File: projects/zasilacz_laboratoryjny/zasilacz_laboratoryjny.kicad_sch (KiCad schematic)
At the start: 33 parts, among them J1 Conn_Point, J2 Conn_Point, J3 Conn_Point, J4 Conn_Point, P1 10kΩ, T1 BC557, T2 BC557, T3 BC547, T4 BC547, T5 BC557, U1 DB207, U2 LM317, U3 Voltmeter_digital, Y1 Buzzer_Piezo_Active

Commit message: zasilacz laboratoryjny v2.0
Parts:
- removed R3: 10kΩ, symbol *Custom_Generic:R
- removed Y1: Buzzer_Piezo_Active, symbol *Custom_Generic:Buzzer_Piezo_Active
- added D4: Yellow, symbol *Custom_Generic:LED
- added T6: BC557, symbol *Custom_Generic:PNP_BJT_BCE
- added Y1: 3V, symbol *Custom_Generic:Buzzer_Magnetic_Active
- D1: value 5V6 -> 3V6
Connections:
- net GNDD: now reaches C1.1 (-), C2.1 (-), C3.2, D3.1 (K), R1.2, R11.2, R5.2, T2.2 (C), T4.3 (E), U1.2 (−)
- net GNDD: now also T6.2 (C); no longer U3.2 (GND)
- net VDC: now reaches C1.2 (+), R4.1, T1.3 (E), U1.1 (+), U2.3 (VI)
- net VDC: now also D1.1 (K), U3.2 (PWR), Y1.1; no longer R2.1, U3.1 (PWR)
- net at C2.2 (+), D2.2 (A): now also R2.2, D4.2 (A); no longer D1.2 (A), T3.1 (C)
- net at C5.2 (+), J3.1 (Pin_1), R10.1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: now also U3.1 (SENSE); no longer U3.3 (SENSE)
- net at C4.1 (-), C5.1 (-), J4.1 (Pin_1)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: now also U3.3 (GND)
- new net: T6.3 (E), Y1.2
- new net: D1.2 (A), R2.1, T6.1 (B)
- new net: D4.1 (K), T3.1 (C)
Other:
- moved on the sheet: C1, C2, C3, C4, C5, D1, D2, D3, P1, R1, R10, R11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

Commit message: Wersja 2.0 po modyfikacjach wynikłych z testowania
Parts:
- added D5: 1N4007, symbol *Custom_Generic:D
- added R12, R3: 10kΩ, symbol *Custom_Generic:R
- added R13, R14: 1kΩ, symbol *Custom_Generic:R
- added T7: BC517, symbol *Custom_Generic:NPN_Darlington_CBE
- added T8: BC547, symbol *Custom_Generic:NPN_BJT_CBE
- C2: value 22μF/25V -> 100μF/25V
- D1: value 3V6 -> 1N4729
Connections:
- net at D2.2 (A), R2.2: no longer C2.2 (+), D4.2 (A)
- net at D1.2 (A), R2.1, T6.1 (B): now also R13.1
- net at R5.1, T3.3 (E), T4.2 (B): now also T8.2 (B)
- net at D4.1 (K): now also T8.1 (C); no longer T3.1 (C)
- net GNDD renamed GND
- net GND: now also R12.2, T8.3 (E)
- net VDC renamed V1
- net V1: now also D5.1 (K), R14.1, T7.1 (C); no longer D1.1 (K), U1.1 (+), U3.2 (PWR), Y1.1
- new net: D4.2 (A), R13.2
- new net: D5.2 (A), R3.1, U1.1 (+)
- new net: R12.1, R3.2, T7.2 (B)
- new net: R14.2, T3.1 (C)
- new net V3: C2.2 (+), D1.1 (K), T7.3 (E), U3.2 (PWR), Y1.1
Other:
- moved on the sheet: C1, C3, C4, C5, D1, D2, D3, D4, P1, R1, R10, R11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

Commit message: preparations for board design in VeeCAD
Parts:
- removed R11: Current sense, symbol *Custom_Generic:R
- added R14, R15: 75Ω, VeeCad:AX3_1N, symbol *Custom_Generic:R
- added R16, R17: 10Ω, VeeCad:AX3_1N, symbol *Custom_Generic:R
- added R18, R19: 22Ω, VeeCad:AX3_1N, symbol *Custom_Generic:R
- added R20: 5,6Ω, VeeCad:AX3_1N, symbol *Custom_Generic:R
- added R21: 2,2Ω, VeeCad:AX3_1N, symbol *Custom_Generic:R
- added R22: 3,9Ω, VeeCad:AX6_2N, symbol *Custom_Generic:R
- added R23: 1Ω, VeeCad:AX6_2N, symbol *Custom_Generic:R
- added R24: 2Ω, VeeCad:AX6_2N, symbol *Custom_Generic:R
- added R25: 0,33Ω, VeeCad:AX6_2N, symbol *Custom_Generic:R
- added R26: 1,5Ω, VeeCad:AX6_2N, symbol *Custom_Generic:R
- added R27: 0Ω, VeeCad:AX1_1N, symbol *Custom_Generic:R
- added SW1: SW_SP8T, VeeCad:SIP9, symbol *Custom_Generic:SW_SP8T
- added SW2: SW_SPST, VeeCad:SIP2, symbol *Custom_Generic:SW_SPST
- C1: footprint (none) -> VeeCad:RA3_6
- C2, C4: footprint (none) -> VeeCad:RA1_2
- C3: footprint (none) -> VeeCad:AX2_1N
- C5: footprint (none) -> VeeCad:RA1_3
- D1, D5: footprint (none) -> VeeCad:AX2_1
- D2, D3, D4: footprint (none) -> VeeCad:SIP2
- J1, J2, J3, J4: footprint (none) -> VeeCad:SIP1
- P1, U3: footprint (none) -> VeeCad:SIP3
- R1, R10, R13, R2, R3, R4, R5, R6, R7, R8, R9: footprint (none) -> VeeCad:AX3_1N
- R11: renamed from R14; footprint (none) -> VeeCad:AX3_1N
- R12: value 10kΩ -> 220kΩ; footprint (none) -> VeeCad:AX3_1N
- T1, T2, T3, T4, T5, T6, T7, T8: footprint (none) -> VeeCad:TO92
- U1: footprint (none) -> VeeCad:DIP4_6
- U2: footprint Package_TO_SOT_THT:TO-220-3_Vertical -> VeeCad:TO220
- Y1: footprint (none) -> VeeCad:BUZR_12
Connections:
- net GND: now also U1.4 (−), R14.2, R15.2, R17.2, R18.2, R19.2, R21.2, R23.2, R25.2, R26.2, R27.2; no longer U1.2 (−)
- net at C4.1 (-), C5.1 (-), J4.1 (Pin_1)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: now also SW1.1
- net at D5.2 (A), R3.1: now also U1.3 (+); no longer U1.1 (+)
- net at J2.1 (Pin_1): now also SW2.2 (B1); no longer U1.4 (∼)
- net at J1.1 (Pin_1): now also U1.1 (∼); no longer U1.3 (∼)
- new net: R20.1, SW1.5
- new net: R20.2, R21.1
- new net: R27.1, SW1.9
- new net: R18.1, R19.1, SW1.4
- new net: R14.1, R15.1, SW1.2
- new net: SW2.1 (A1), U1.2 (∼)
- new net: R24.1, SW1.7
- new net: R24.2, R25.1
- new net: R22.1, SW1.6
- new net: R22.2, R23.1
- new net: R26.1, SW1.8
- new net: R16.2, R17.1
- new net: R16.1, SW1.3
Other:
- note added: "100mA"
- note added: "150mA"
- note added: "20mA"
- note added: "250mA"
- note added: "500mA"
- note added: "50mA"
- note added: "750mA"
- note added: "AC / DC"
- note added: "No OCP"
- note removed: "AC 12V"
- moved on the sheet: C1, C2, C3, C4, C5, D1, D2, D3, D4, D5, P1, R1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

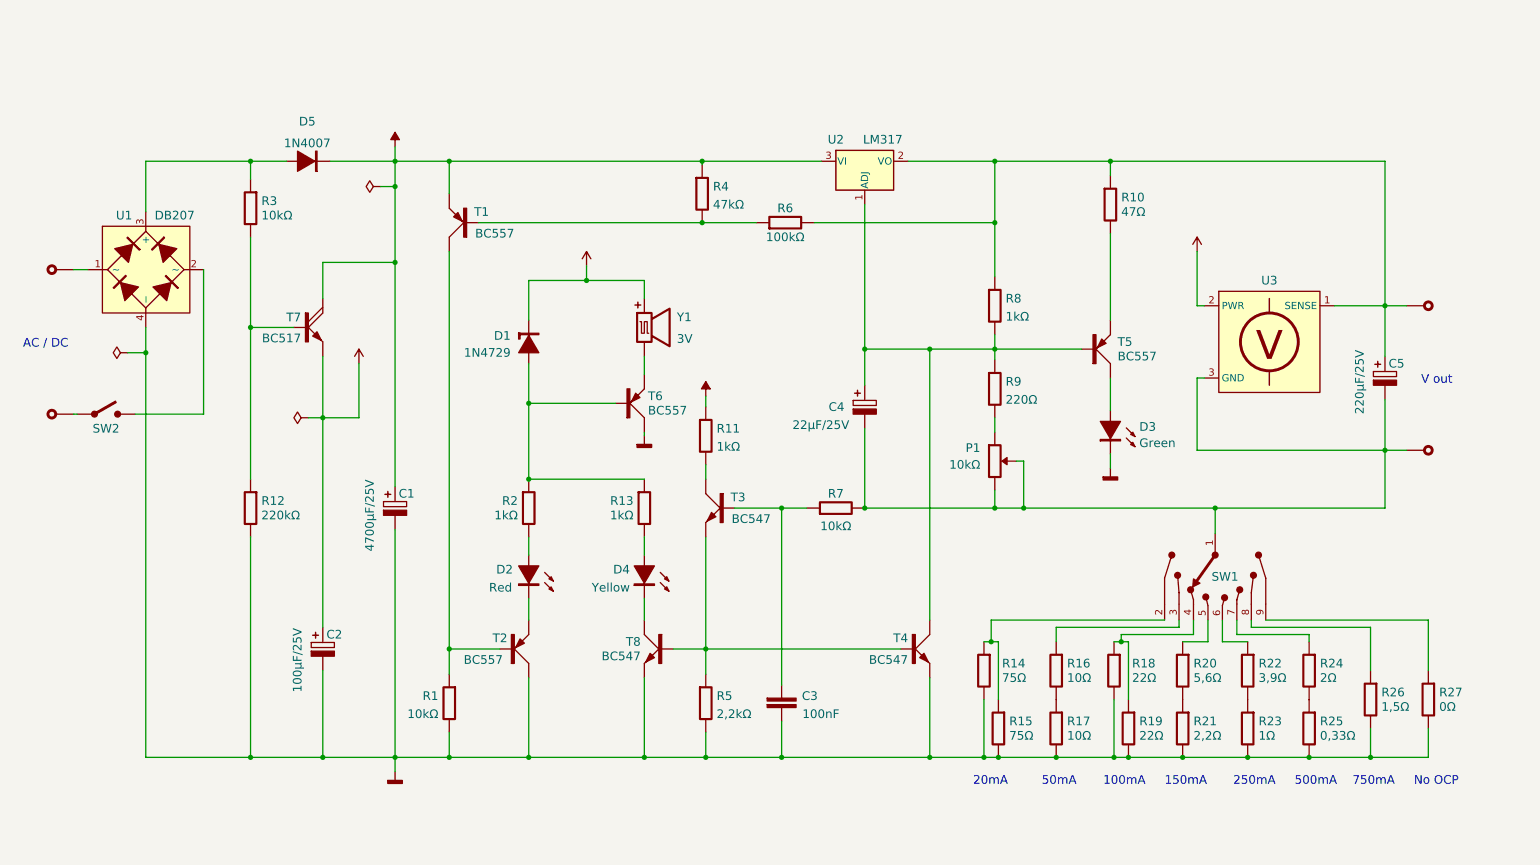
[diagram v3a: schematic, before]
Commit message: started veecad layout for zasilacz_laboratoryjny, some small stuff elsewhere
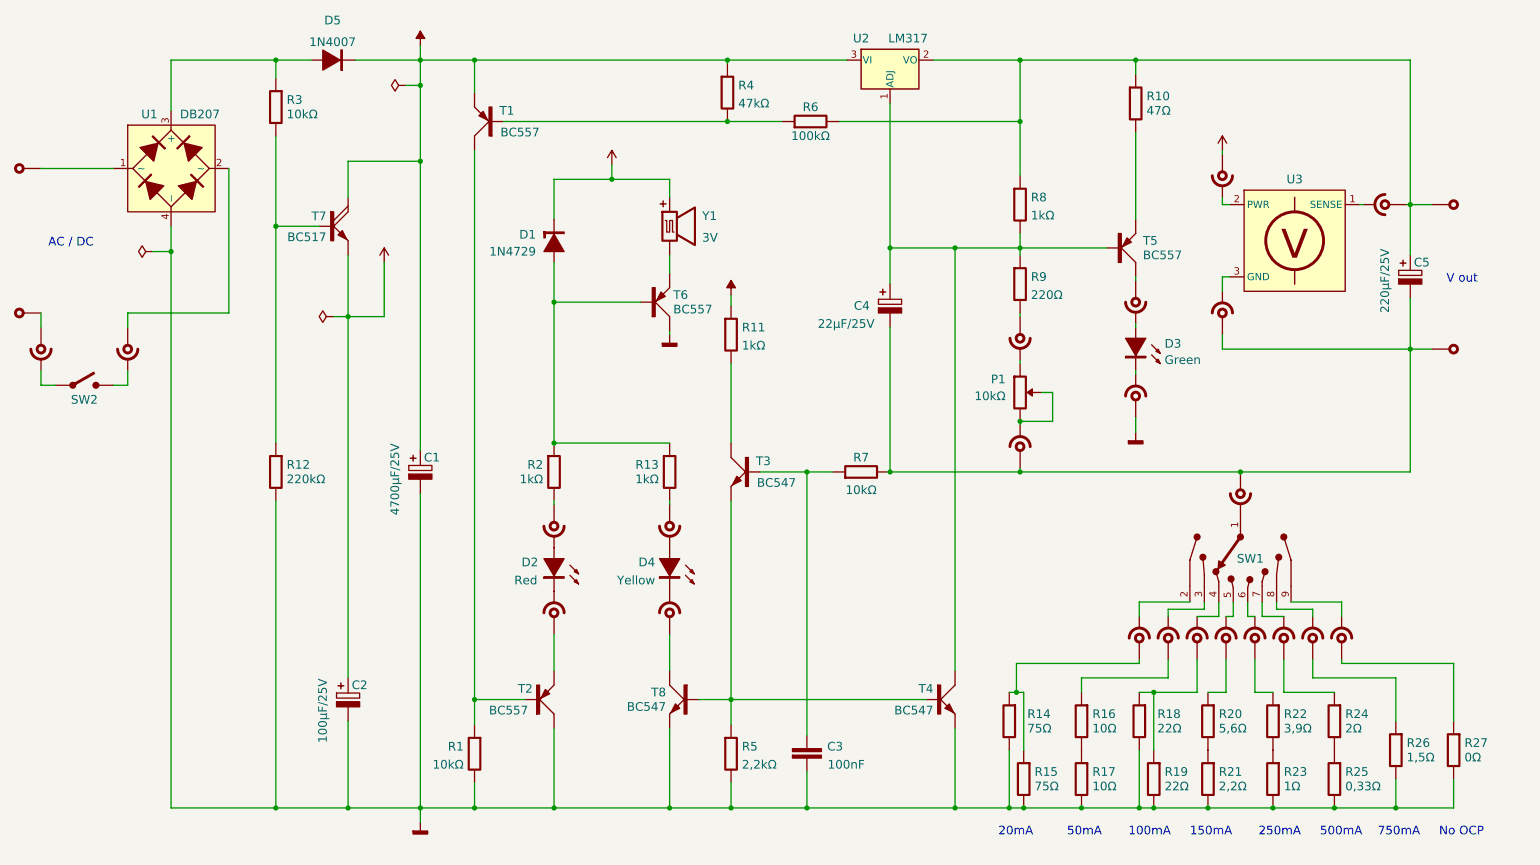
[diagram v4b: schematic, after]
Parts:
- added J10: VDO_LED+, VeeCad:SIP1, symbol *Custom_Generic:Conn_Point_M
- added J11, J14, J15, J17, J19, J21, J24, J26, J28, J29, J31, J33, J35, J37, J39, J41, J43, J46, J48, J5, J8, J9: Conn_Point_1, symbol *Custom_Generic:Conn_Point_F
- added J12: VDO_LED−, VeeCad:SIP1, symbol *Custom_Generic:Conn_Point_M
- added J13: OCP_LED+, VeeCad:SIP1, symbol *Custom_Generic:Conn_Point_M
- added J16: OCP_LED−, VeeCad:SIP1, symbol *Custom_Generic:Conn_Point_M
- added J18: VPOT_1, VeeCad:SIP1, symbol *Custom_Generic:Conn_Point_M
- added J20: VPOT_2, VeeCad:SIP1, symbol *Custom_Generic:Conn_Point_M
- added J22: PWR_LED+, VeeCad:SIP1, symbol *Custom_Generic:Conn_Point_M
- added J23: PWR_LED−, VeeCad:SIP1, symbol *Custom_Generic:Conn_Point_M
- added J25: OCP_SW1, VeeCad:SIP1, symbol *Custom_Generic:Conn_Point_M
- added J27: OCP_SW2, VeeCad:SIP1, symbol *Custom_Generic:Conn_Point_M
- added J30: OCP_SW3, VeeCad:SIP1, symbol *Custom_Generic:Conn_Point_M
- added J32: VM_PWR, VeeCad:SIP1, symbol *Custom_Generic:Conn_Point_M
- added J34: VM_GND, VeeCad:SIP1, symbol *Custom_Generic:Conn_Point_M
- added J36: OCP_SW4, VeeCad:SIP1, symbol *Custom_Generic:Conn_Point_M
- added J38: OCP_SW_IN, VeeCad:SIP1, symbol *Custom_Generic:Conn_Point_M
- added J40: OCP_SW5, VeeCad:SIP1, symbol *Custom_Generic:Conn_Point_M
- added J42: OCP_SW6, VeeCad:SIP1, symbol *Custom_Generic:Conn_Point_M
- added J44: OCP_SW7, VeeCad:SIP1, symbol *Custom_Generic:Conn_Point_M
- added J45: OCP_SW8, VeeCad:SIP1, symbol *Custom_Generic:Conn_Point_M
- added J47: VM_SEN, VeeCad:SIP1, symbol *Custom_Generic:Conn_Point_M
- added J6: PWR_SW1, VeeCad:SIP1, symbol *Custom_Generic:Conn_Point_M
- added J7: PWR_SW2, VeeCad:SIP1, symbol *Custom_Generic:Conn_Point_M
- C3: footprint VeeCad:AX2_1N -> VeeCad:AX1_1N
- D2, D3, D4, SW2: footprint VeeCad:SIP2 -> (none)
- J1, J2: value Conn_Point -> AC_IN; symbol *Custom_Generic:Conn_Point -> *Custom_Generic:Conn_Point_M
- J3: value Conn_Point -> VOUT+; symbol *Custom_Generic:Conn_Point -> *Custom_Generic:Conn_Point_M
- J4: value Conn_Point -> VOUT−; symbol *Custom_Generic:Conn_Point -> *Custom_Generic:Conn_Point_M
- P1, U3: footprint VeeCad:SIP3 -> (none)
- R16, R17, R20, R21: footprint VeeCad:AX3_1N -> VeeCad:VERTAX_1N
- R22, R23, R24, R25, R26: footprint VeeCad:AX6_2N -> VeeCad:VERTAX2_1N
- SW1: footprint VeeCad:SIP9 -> (none)
- U1: footprint VeeCad:DIP4_6 -> VeeCad:DIP4_DB
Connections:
- net GND: now also J23.1 (Pin_1); no longer D3.1 (K)
- net V3: now also J32.1 (Pin_1); no longer U3.2 (PWR)
- net at C5.2 (+), J3.1 (Pin_1), R10.1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: now also J47.1 (Pin_1); no longer U3.1 (SENSE)
- net at R20.1: now also J36.1 (Pin_1); no longer SW1.5
- net at R27.1: now also J45.1 (Pin_1); no longer SW1.9
- net at R18.1, R19.1: now also J30.1 (Pin_1); no longer SW1.4
- net at C4.1 (-), C5.1 (-), J4.1 (Pin_1)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: now also J20.1 (Pin_1), J34.1 (Pin_1), J38.1 (Pin_1); no longer P1.2, P1.3, SW1.1, U3.3 (GND)
- net at R14.1, R15.1: now also J25.1 (Pin_1); no longer SW1.2
- net at U1.2 (∼): now also J7.1 (Pin_1); no longer SW2.1 (A1)
- net at SW2.2 (B1): now also J5.1 (Pin_1); no longer J2.1 (Pin_1)
- net at R24.1: now also J42.1 (Pin_1); no longer SW1.7
- net at SW1.6: now also J39.1 (Pin_1); no longer R22.1
- net at T8.1 (C): now also J16.1 (Pin_1); no longer D4.1 (K)
- net at P1.1: now also J17.1 (Pin_1); no longer R9.2
- net at R13.2: now also J13.1 (Pin_1); no longer D4.2 (A)
- net at D3.2 (A): now also J21.1 (Pin_1); no longer T5.2 (C)
- net at D2.2 (A): now also J9.1 (Pin_1); no longer R2.2
- net at D2.1 (K): now also J11.1 (Pin_1); no longer T2.3 (E)
- net at SW1.8: now also J43.1 (Pin_1); no longer R26.1
- net at R16.1: now also J27.1 (Pin_1); no longer SW1.3
- new net: J31.1 (Pin_1), U3.2 (PWR)
- new net: J37.1 (Pin_1), SW1.1
- new net: J29.1 (Pin_1), SW1.4
- new net: J8.1 (Pin_1), SW2.1 (A1)
- new net: J40.1 (Pin_1), R22.1
- new net: J41.1 (Pin_1), SW1.7
- new net: J19.1 (Pin_1), P1.2, P1.3
- new net: J33.1 (Pin_1), U3.3 (GND)
- new net: J12.1 (Pin_1), T2.3 (E)
- new net: D3.1 (K), J24.1 (Pin_1)
- new net: D4.1 (K), J15.1 (Pin_1)
- new net: J10.1 (Pin_1), R2.2
- new net: J48.1 (Pin_1), U3.1 (SENSE)
- new net: J2.1 (Pin_1), J6.1 (Pin_1)
- new net: J35.1 (Pin_1), SW1.5
- new net: D4.2 (A), J14.1 (Pin_1)
- new net: J44.1 (Pin_1), R26.1
- new net: J18.1 (Pin_1), R9.2
- new net: J22.1 (Pin_1), T5.2 (C)
- new net: J28.1 (Pin_1), SW1.3
- new net: J26.1 (Pin_1), SW1.2
- new net: J46.1 (Pin_1), SW1.9
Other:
- moved on the sheet: C1, C2, C3, C4, C5, D1, D2, D3, D4, D5, P1, R1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

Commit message: beautify some symbols, power supply WIP
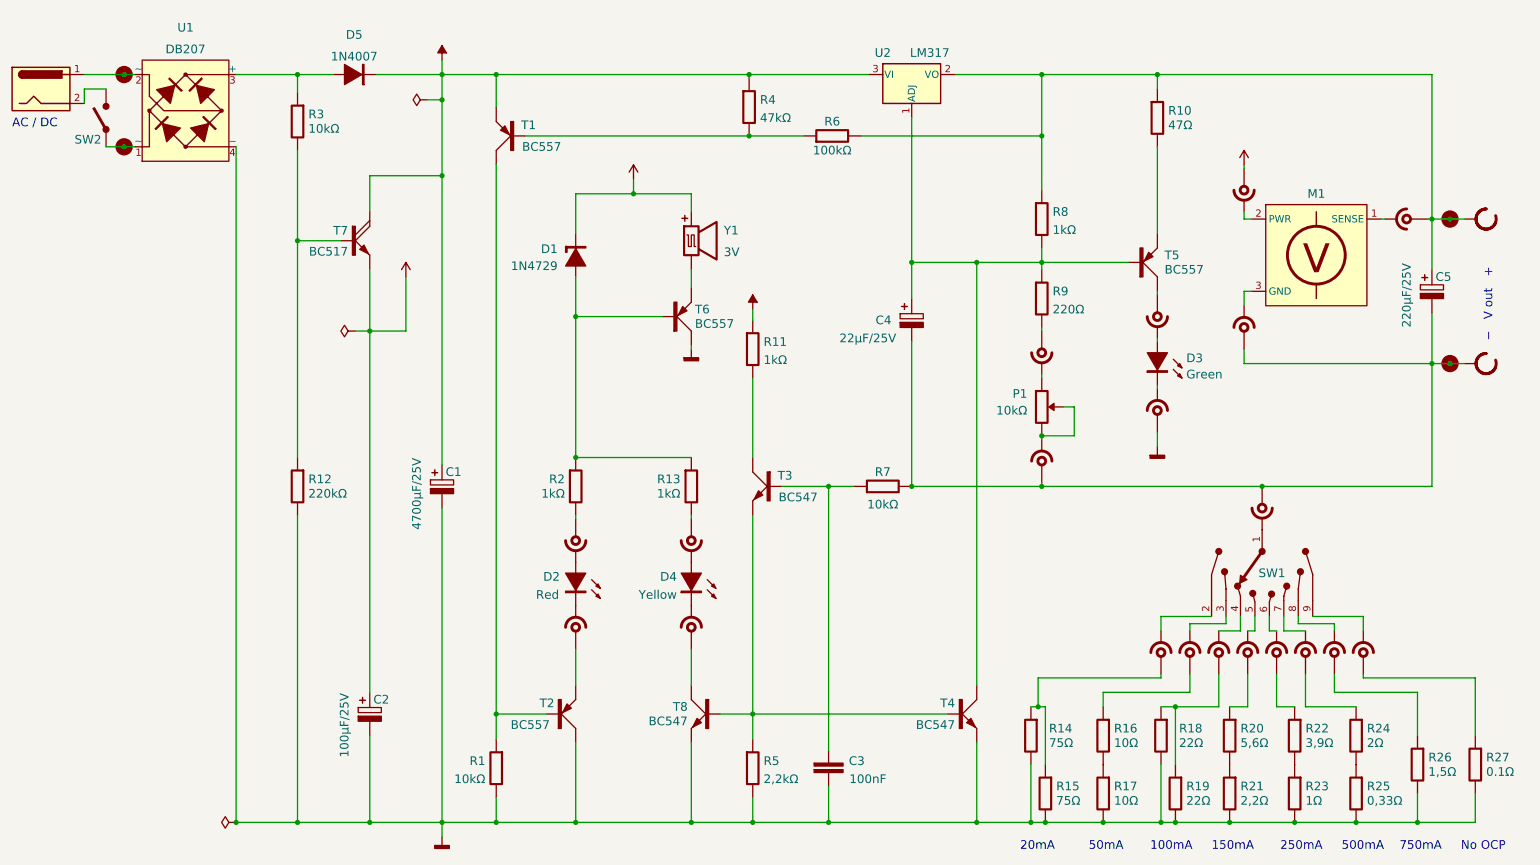
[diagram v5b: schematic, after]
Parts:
- removed J1, J2: AC_IN, VeeCad:SIP1, symbol *Custom_Generic:Conn_Point_M
- removed J3: VOUT+, VeeCad:SIP1, symbol *Custom_Generic:Conn_Point_M
- removed J4: VOUT−, VeeCad:SIP1, symbol *Custom_Generic:Conn_Point_M
- removed J5, J8: Conn_Point_1, symbol *Custom_Generic:Conn_Point_F
- removed J6: PWR_SW1, VeeCad:SIP1, symbol *Custom_Generic:Conn_Point_M
- removed J7: PWR_SW2, VeeCad:SIP1, symbol *Custom_Generic:Conn_Point_M
- added J1: OUT+, VeeCad:WIREPOINT, symbol *Custom_Generic:Wire_Solderpoint
- added J100: BARREL JACK, symbol Connector:Barrel_Jack
- added J101, J102: BANANA JACK, symbol *Custom_Generic:Conn_Jack
- added J2: OUT-, VeeCad:WIREPOINT, symbol *Custom_Generic:Wire_Solderpoint
- added J3: PWRIN, VeeCad:WIREPOINT, symbol *Custom_Generic:Wire_Solderpoint
- added J4: PWRSW, VeeCad:WIREPOINT, symbol *Custom_Generic:Wire_Solderpoint
- D5: footprint VeeCad:AX2_1 -> VeeCad:VERTAX_1U
- J10: renamed from J23; value PWR_LED− -> PWRL−
- J103: renamed from J9; value Conn_Point_1 -> OFF_BOARD
- J104: renamed from J11; value Conn_Point_1 -> OFF_BOARD
- J105: renamed from J14; value Conn_Point_1 -> OFF_BOARD
- J106: renamed from J15; value Conn_Point_1 -> OFF_BOARD
- J107: renamed from J17; value Conn_Point_1 -> OFF_BOARD
- J108: renamed from J19; value Conn_Point_1 -> OFF_BOARD
- J109: renamed from J21; value Conn_Point_1 -> OFF_BOARD
- J11: renamed from J18; value VPOT_1 -> VSET1
- J110: renamed from J24; value Conn_Point_1 -> OFF_BOARD
- J111: renamed from J26; value Conn_Point_1 -> OFF_BOARD
- J112: renamed from J28; value Conn_Point_1 -> OFF_BOARD
- J113: renamed from J29; value Conn_Point_1 -> OFF_BOARD
- J114: renamed from J31; value Conn_Point_1 -> OFF_BOARD
- J115: renamed from J33; value Conn_Point_1 -> OFF_BOARD
- J116: renamed from J35; value Conn_Point_1 -> OFF_BOARD
- J117: renamed from J37; value Conn_Point_1 -> OFF_BOARD
- J118: renamed from J39; value Conn_Point_1 -> OFF_BOARD
- J119: renamed from J41; value Conn_Point_1 -> OFF_BOARD
- J12: renamed from J20; value VPOT_2 -> VSET2
- J120: renamed from J43; value Conn_Point_1 -> OFF_BOARD
- J121: renamed from J46; value Conn_Point_1 -> OFF_BOARD
- J122: renamed from J48; value Conn_Point_1 -> OFF_BOARD
- J13: value OCP_LED+ -> OCPL+
- J14: renamed from J16; value OCP_LED− -> OCPL−
- J15: renamed from J10; value VDO_LED+ -> VDOL+
- J16: renamed from J12; value VDO_LED− -> VDOL−
- J17: renamed from J25; value OCP_SW1 -> OCP1
- J18: renamed from J27; value OCP_SW2 -> OCP2
- J19: renamed from J30; value OCP_SW3 -> OCP3
- J20: renamed from J36; value OCP_SW4 -> OCP4
- J21: renamed from J40; value OCP_SW5 -> OCP5
- J22: renamed from J42; value OCP_SW6 -> OCP6
- J23: renamed from J44; value OCP_SW7 -> OCP7
- J24: renamed from J45; value OCP_SW8 -> OCP8
- J5: renamed from J47; value VM_SEN -> VMPROBE
- J6: renamed from J32; value VM_PWR -> VMPWR
- J7: renamed from J34; value VM_GND -> VMGND
- J8: renamed from J38; value OCP_SW_IN -> OCP0
- J9: renamed from J22; value PWR_LED+ -> PWRL+
- M1: renamed from U3; value Voltmeter_digital -> DIGITAL_VM; symbol *Custom_Generic:Voltmeter_digital -> *Custom_Generic:VM_DIGITAL
- R10, R9: footprint VeeCad:AX3_1N -> VeeCad:VERTAX_2N
- R13: footprint VeeCad:AX3_1N -> VeeCad:VERTAX_2N_180
- R2: footprint VeeCad:AX3_1N -> VeeCad:VERTAX_1N_180
- R27: value 0Ω -> 0.1Ω; footprint VeeCad:AX1_1N -> VeeCad:VERTAX2_1N
- R8: footprint VeeCad:AX3_1N -> VeeCad:VERTAX_1N
- T1, T2, T6: symbol *Custom_Generic:PNP_BJT_BCE -> *Custom_Generic:PNP_BJT_CBE
- T5: footprint VeeCad:TO92 -> VeeCad:TO92_ALT2; symbol *Custom_Generic:PNP_BJT_BCE -> *Custom_Generic:PNP_BJT_CBE
- T7: symbol *Custom_Generic:NPN_Darlington_CBE -> *Custom_Generic:NPN_Darlington_EBC
- U1: symbol Custom_Generic:D_bridge -> Custom_Generic:D_bridge_DIP
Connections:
- net GND: now also T2.1 (C), T6.1 (C); no longer T2.2 (C), T6.2 (C)
- net V1: now also T7.3 (C); no longer T7.1 (C)
- net V3: now also T7.1 (E); no longer T7.3 (E)
- net at U1.2 (∼): now also J100.1, J3.1 (wire/board)
- net at C5.2 (+), J5.1 (Pin_1), R10.1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: now also J1.1 (wire/board), J101.1 (Pin_1)
- net at C4.1 (-), C5.1 (-), J12.1 (Pin_1)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: now also J102.1 (Pin_1), J2.1 (wire/board)
- net at SW2.1 (A1): now also J100.2
- net at SW2.2 (B1): now also U1.1 (∼), J4.1 (wire/board)
- net at D1.2 (A), R13.1, R2.1: now also T6.2 (B); no longer T6.1 (B)
- net at C4.2 (+), R8.2, R9.1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: now also T5.2 (B); no longer T5.1 (B)
- net at R4.2, R6.1: now also T1.2 (B); no longer T1.1 (B)
- net at J9.1 (Pin_1): now also T5.1 (C); no longer T5.2 (C)
- new net: R1.1, T1.1 (C), T2.2 (B)
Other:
- note added: "− V out +"
- note removed: "V out"
- moved on the sheet: C1, C2, C3, C4, C5, D1, D2, D3, D4, D5, M1, P1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
